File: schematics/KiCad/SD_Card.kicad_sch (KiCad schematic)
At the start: 9 parts, among them J7 Micro_SD_Card_Det_Hirose_DM3AT, U14 74HC4050

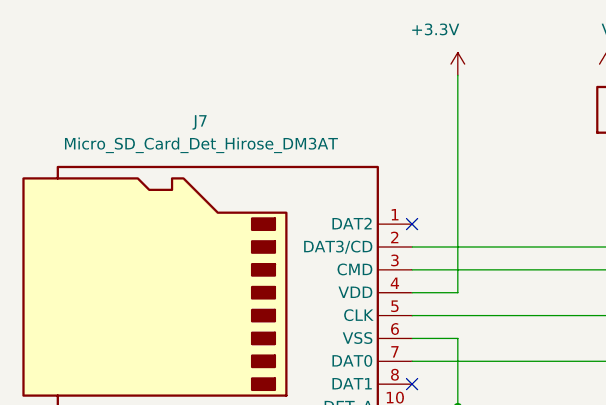
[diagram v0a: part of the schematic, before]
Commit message: Changed USB power line connection.
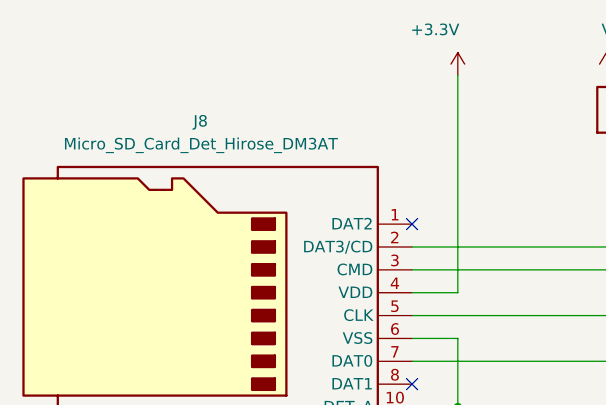
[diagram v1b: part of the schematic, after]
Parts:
- renumbered J7 to J8
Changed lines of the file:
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@@
   (symbol (lib_id "power:GND") (at 125.73 71.12 0) (unit 1)
     (in_bom yes) (on_board yes) (dnp no)
-    (property "Reference" "#PWR075" (at 125.73 77.47 0)
+    (property "Reference" "#PWR077" (at 125.73 77.47 0)
       (effects (font (size 1.27 1.27)) hide)
     )
@@
       (project "Z80ATmega128"
         (path "/8c0ff608-9e5b-458c-8fa7-b9973ff97e88/07de70fd-23a2-48ea-a888-9c9311d1e8a8"
-          (reference "#PWR075") (unit 1)
+          (reference "#PWR077") (unit 1)
         )
       )
@@
   (symbol (lib_id "power:GND") (at 73.66 96.52 0) (unit 1)
     (in_bom yes) (on_board yes) (dnp no) (fields_autoplaced)
-    (property "Reference" "#PWR076" (at 73.66 102.87 0)
+    (property "Reference" "#PWR078" (at 73.66 102.87 0)
       (effects (font (size 1.27 1.27)) hide)
     )
@@
       (project "Z80ATmega128"
         (path "/8c0ff608-9e5b-458c-8fa7-b9973ff97e88/07de70fd-23a2-48ea-a888-9c9311d1e8a8"
-          (reference "#PWR076") (unit 1)
+          (reference "#PWR078") (unit 1)
         )
       )
@@
   (symbol (lib_id "power:GND") (at 72.39 140.97 0) (unit 1)
     (in_bom yes) (on_board yes) (dnp no) (fields_autoplaced)
-    (property "Reference" "#PWR079" (at 72.39 147.32 0)
+    (property "Reference" "#PWR081" (at 72.39 147.32 0)
       (effects (font (size 1.27 1.27)) hide)
     )
@@
       (project "Z80ATmega128"
         (path "/8c0ff608-9e5b-458c-8fa7-b9973ff97e88/07de70fd-23a2-48ea-a888-9c9311d1e8a8"
-          (reference "#PWR079") (unit 1)
+          (reference "#PWR081") (unit 1)
         )
       )
@@
   (symbol (lib_id "power:+3.3V") (at 46.99 118.11 0) (unit 1)
     (in_bom yes) (on_board yes) (dnp no) (fields_autoplaced)
-    (property "Reference" "#PWR078" (at 46.99 121.92 0)
+    (property "Reference" "#PWR080" (at 46.99 121.92 0)
       (effects (font (size 1.27 1.27)) hide)
     )
@@
       (project "Z80ATmega128"
         (path "/8c0ff608-9e5b-458c-8fa7-b9973ff97e88/07de70fd-23a2-48ea-a888-9c9311d1e8a8"
-          (reference "#PWR078") (unit 1)
+          (reference "#PWR080") (unit 1)
         )
       )
@@
   (symbol (lib_id "power:+3.3V") (at 73.66 40.64 0) (unit 1)
     (in_bom yes) (on_board yes) (dnp no)
-    (property "Reference" "#PWR072" (at 73.66 44.45 0)
+    (property "Reference" "#PWR074" (at 73.66 44.45 0)
       (effects (font (size 1.27 1.27)) hide)
     )
@@
       (project "Z80ATmega128"
         (path "/8c0ff608-9e5b-458c-8fa7-b9973ff97e88/07de70fd-23a2-48ea-a888-9c9311d1e8a8"
-          (reference "#PWR072") (unit 1)
+          (reference "#PWR074") (unit 1)
         )
       )
@@
   (symbol (lib_id "Connector:Micro_SD_Card_Det_Hirose_DM3AT") (at 45.72 67.31 0) (mirror y) (unit 1)
     (in_bom yes) (on_board yes) (dnp no) (fields_autoplaced)
-    (property "Reference" "J7" (at 45.085 45.72 0)
+    (property "Reference" "J8" (at 45.085 45.72 0)
       (effects (font (size 1.27 1.27)))
     )
@@
       (project "Z80ATmega128"
         (path "/8c0ff608-9e5b-458c-8fa7-b9973ff97e88/07de70fd-23a2-48ea-a888-9c9311d1e8a8"
-          (reference "J7") (unit 1)
+          (reference "J8") (unit 1)
         )
       )
@@
   (symbol (lib_id "power:VCC") (at 125.73 40.64 0) (unit 1)
     (in_bom yes) (on_board yes) (dnp no) (fields_autoplaced)
-    (property "Reference" "#PWR074" (at 125.73 44.45 0)
+    (property "Reference" "#PWR076" (at 125.73 44.45 0)
       (effects (font (size 1.27 1.27)) hide)
     )
@@
       (project "Z80ATmega128"
         (path "/8c0ff608-9e5b-458c-8fa7-b9973ff97e88/07de70fd-23a2-48ea-a888-9c9311d1e8a8"
-          (reference "#PWR074") (unit 1)
+          (reference "#PWR076") (unit 1)
         )
       )
@@
   (symbol (lib_id "power:GND") (at 46.99 143.51 0) (unit 1)
     (in_bom yes) (on_board yes) (dnp no) (fields_autoplaced)
-    (property "Reference" "#PWR080" (at 46.99 149.86 0)
+    (property "Reference" "#PWR082" (at 46.99 149.86 0)
       (effects (font (size 1.27 1.27)) hide)
     )
@@
       (project "Z80ATmega128"
         (path "/8c0ff608-9e5b-458c-8fa7-b9973ff97e88/07de70fd-23a2-48ea-a888-9c9311d1e8a8"
-          (reference "#PWR080") (unit 1)
+          (reference "#PWR082") (unit 1)
         )
       )
@@
   (symbol (lib_id "power:GND") (at 148.59 100.33 0) (unit 1)
     (in_bom yes) (on_board yes) (dnp no) (fields_autoplaced)
-    (property "Reference" "#PWR077" (at 148.59 106.68 0)
+    (property "Reference" "#PWR079" (at 148.59 106.68 0)
       (effects (font (size 1.27 1.27)) hide)
     )
@@
       (project "Z80ATmega128"
         (path "/8c0ff608-9e5b-458c-8fa7-b9973ff97e88/07de70fd-23a2-48ea-a888-9c9311d1e8a8"
-          (reference "#PWR077") (unit 1)
+          (reference "#PWR079") (unit 1)
         )
       )
@@
   (symbol (lib_id "power:VCC") (at 90.17 40.64 0) (unit 1)
     (in_bom yes) (on_board yes) (dnp no)
-    (property "Reference" "#PWR073" (at 90.17 44.45 0)
+    (property "Reference" "#PWR075" (at 90.17 44.45 0)
       (effects (font (size 1.27 1.27)) hide)
     )
@@
       (project "Z80ATmega128"
         (path "/8c0ff608-9e5b-458c-8fa7-b9973ff97e88/07de70fd-23a2-48ea-a888-9c9311d1e8a8"
-          (reference "#PWR073") (unit 1)
-        )
-      )
+          (reference "#PWR075") (unit 1)
+        )
+      )

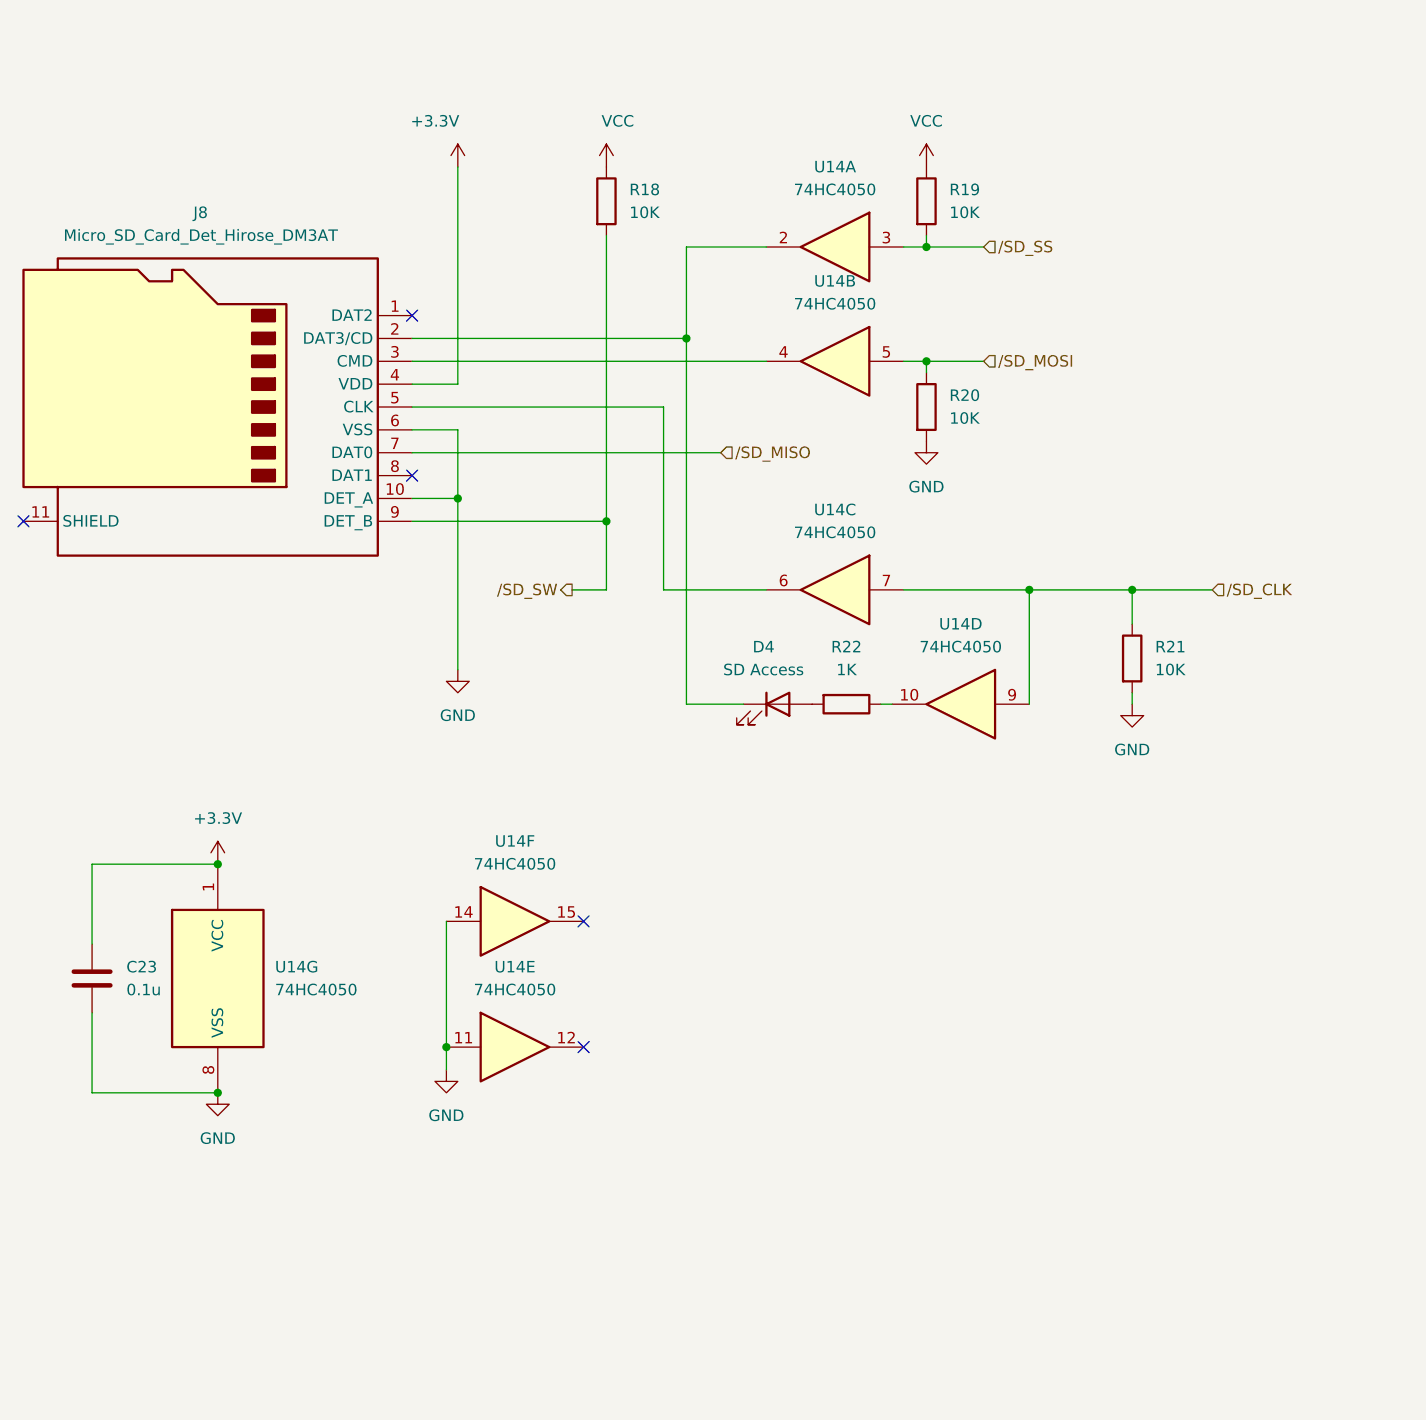
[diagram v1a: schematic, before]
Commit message: Update Reset circuit and Serial interface
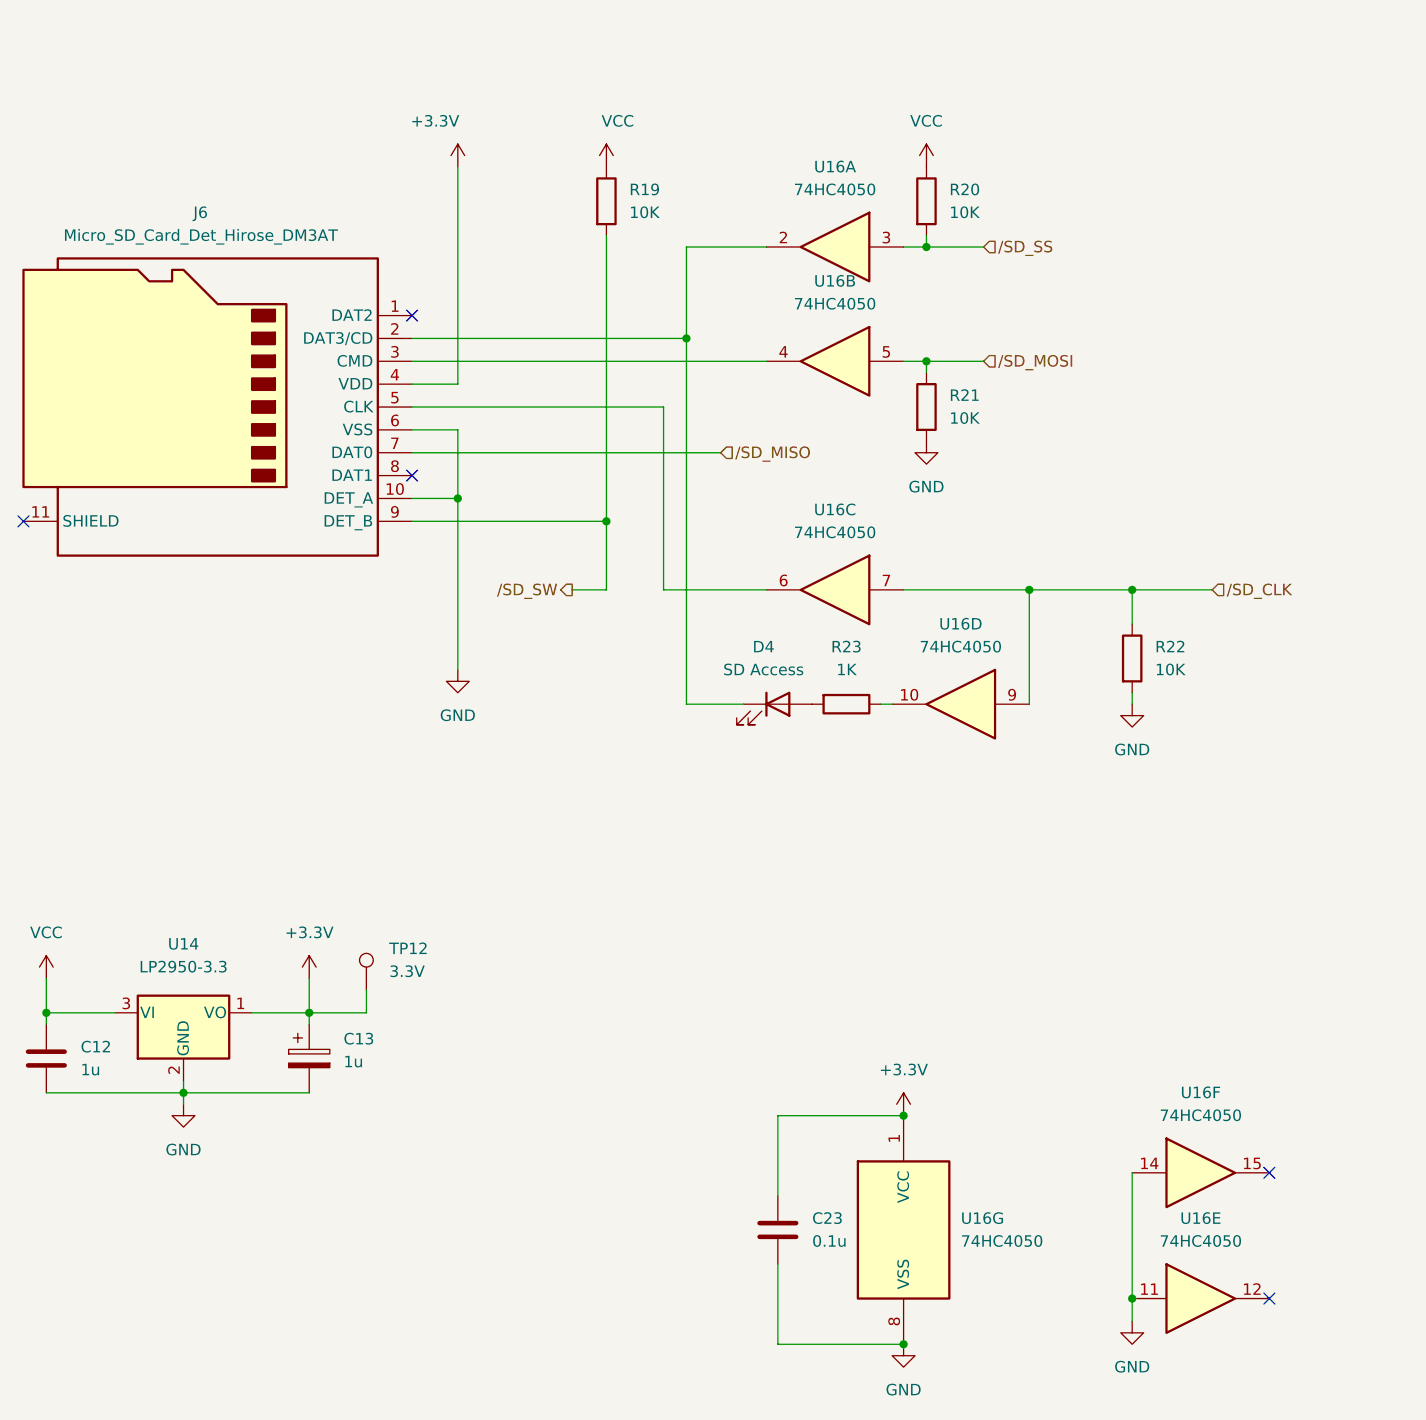
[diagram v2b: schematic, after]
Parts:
- added C12: 1u, Capacitor_THT:CP_Radial_Tantal_D5.0mm_P2.50mm, symbol Device:C
- added C13: 1u, Capacitor_THT:CP_Radial_Tantal_D5.0mm_P2.50mm, symbol Device:C_Polarized
- added TP12: 3.3V, TestPoint:TestPoint_Loop_D2.50mm_Drill1.0mm, symbol Connector:TestPoint
- added U14: LP2950-3.3, Package_TO_SOT_THT:TO-92_Inline, symbol Regulator_Linear:LP2950-3.3_TO92
- renumbered J8 to J6, R18 to R19, R19 to R20, R20 to R21, R21 to R22, R22 to R23, U14 to U16
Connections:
- net +3.3V: now also C13.1, TP12.1, U14.1 (VO)
- net GND: now also C12.2, C13.2, U14.2 (GND)
- net VCC: now also C12.1, U14.3 (VI)
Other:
- moved on the sheet: C23, U16E, U16F, U16G
